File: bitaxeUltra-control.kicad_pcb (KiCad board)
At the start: 4 copper layers, 56.5 x 99.8 mm, 137 parts, among them J1 54-00164, J2 Conn_01x02, J3 Conn_01x05, J4 Conn_01x04, J5 TC2030-IDC, J7 Conn_01x02, J8 USB_C_Receptacle_USB2.0, J9 Conn_01x04, Q1 CSD17311Q5, Q2 CSD17311Q5, Q4 2N7002K, SW1 GT-TC029B-H025-L1N, SW2 GT-TC029B-H025-L1N, U1 25MHz, U10 DS4432U+, U11 RT9080-33GJ5, U12 ESP32-S3-WROOM-1, U14 BM1366_mode1, U2 TXB0104RGYR, U5 MCP1824T-1802E, U6 MCP1824T-0802E, U7 EMC2101, U8 INA260, U9 TPS40305, Y1 32.768kHz

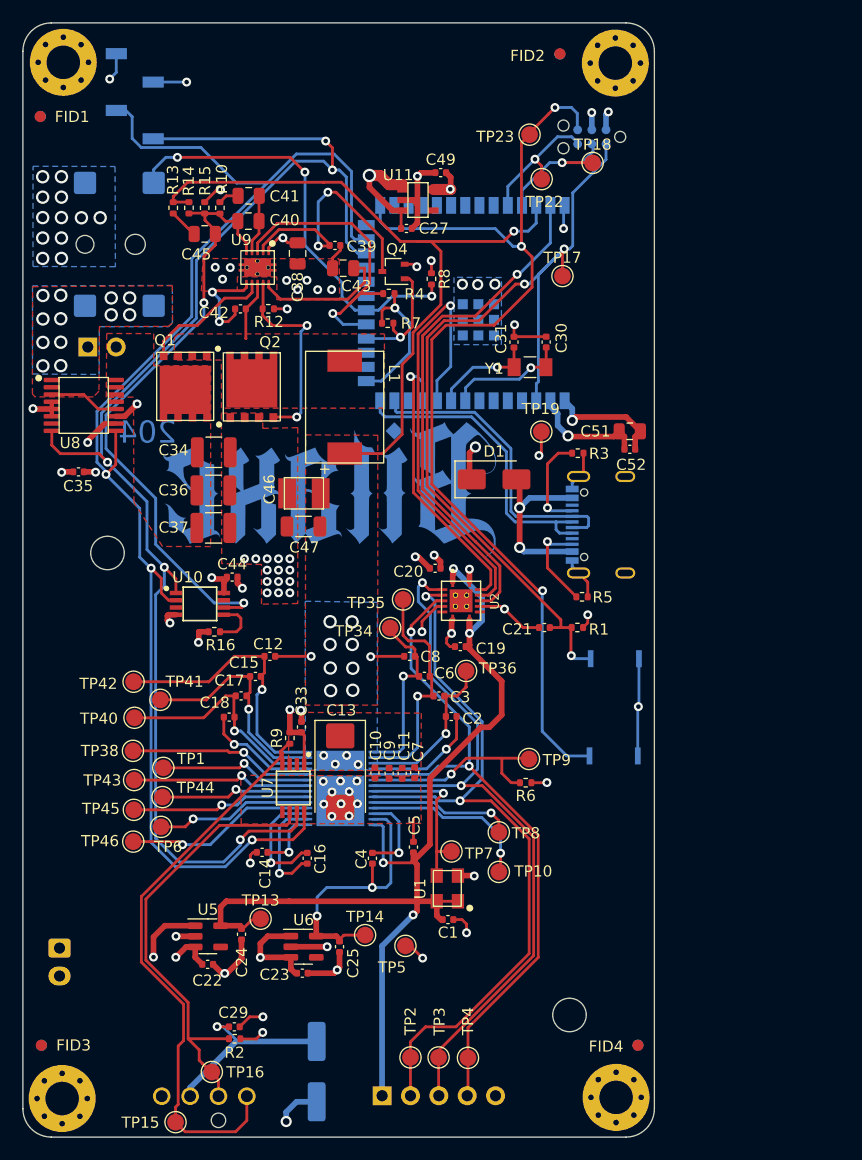
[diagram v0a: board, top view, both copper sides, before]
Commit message: revert  to 4 layer-board routing
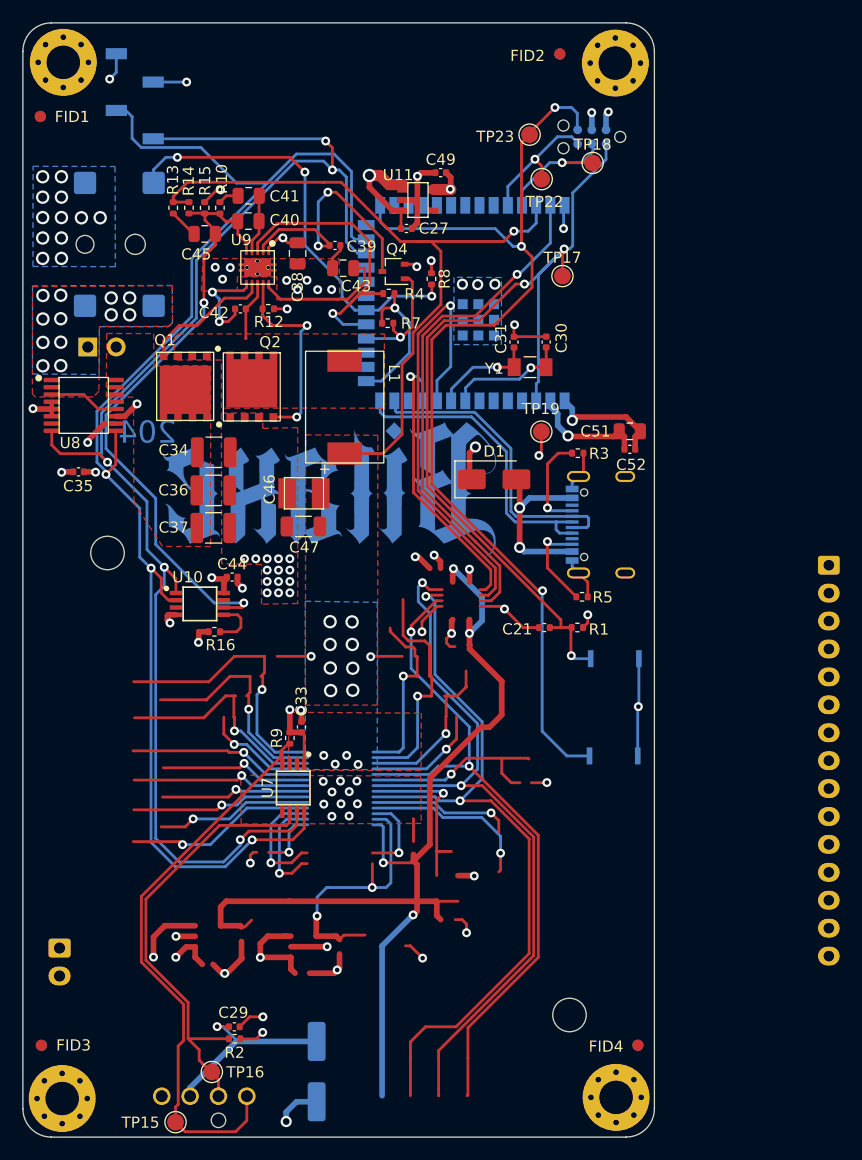
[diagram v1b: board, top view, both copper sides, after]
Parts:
- removed C1, C19, C20, C7, C9: 0.1uF, Capacitor_SMD:C_0402_1005Metric
- removed C10, C11, C12, C14, C15, C16, C17, C18, C2, C22, C23, C24, C25, C3, C4, C5, C6, C8: 1uF, Capacitor_SMD:C_0402_1005Metric
- removed C13: 330uF, Capacitor_Tantalum_SMD:CP_EIA-7343-31_Kemet-D_Pad2.25x2.55mm_HandSolder
- removed R6: 10k, Resistor_SMD:R_0402_1005Metric
- removed TP1, TP10, TP13, TP14, TP2, TP3, TP34, TP35, TP36, TP38, TP4, TP40, TP41, TP42, TP43, TP44, TP45, TP46, TP5, TP6, TP7, TP8, TP9: TestPoint, TestPoint:TestPoint_Pad_D1.5mm
- removed U1: 25MHz, bitaxe:O 25,0-JO32-B-1V3-1-T1-LF
- removed U14: BM1366_mode1, bitaxe:BM1366
- removed U2: TXB0104RGYR, bitaxe:TXB0104
- removed U5: MCP1824T-1802E, Package_TO_SOT_SMD:SOT-23-5
- removed U6: MCP1824T-0802E, Package_TO_SOT_SMD:SOT-23-5
- J3: value Conn_01x05 -> Conn_01x15; footprint Connector_PinHeader_2.54mm:PinHeader_1x05_P2.54mm_Vertical -> Connector_JST:JST_XA_B15B-XASK-1_1x15_P2.50mm_Vertical
- moved J3 62.1 mm to (149.4, 96.1)
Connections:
- J3 pad 1: /BM1366/1V8 -> /RST
- J3 pad 2: /BM1366/CI -> /TX
- J3 pad 3: /BM1366/RO -> /RX
- J3 pad 4: /BM1366/RST_N -> unconnected-(J3-Pin_4-Pad4)
- J3 pad 5: GND -> /5V
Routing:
- net (no net): track 0.00 -> 327.1 mm, vias 0 -> 21
- net /RST: track 46.2 -> 140.3 mm, vias 1 -> 5
- net /BM1366/1V8: track 94.1 -> 0.00 mm, vias 4 -> 0
- net /BM1366/VDD1_1: track 25.2 -> 0.00 mm, vias 1 -> 0
- net /BM1366/0V8: track 24.5 -> 0.00 mm, vias 2 -> 0
- net /BM1366/VDD3_1: track 20.8 -> 0.00 mm, vias 1 -> 0
- net /BM1366/VDD2_0: track 20.7 -> 0.00 mm, vias 1 -> 0
- net /BM1366/VDD2_1: track 20.3 -> 0.00 mm, vias 1 -> 0
- net /BM1366/BI: track 18.2 -> 0.00 mm, vias 1 -> 0
- net /BM1366/PIN_MODE: track 17.1 -> 0.00 mm, vias 1 -> 0
- net /BM1366/NRSTO: track 16.5 -> 0.00 mm, vias 1 -> 0
- net /BM1366/VDD1_0: track 16.2 -> 0.00 mm, vias 1 -> 0
- net /BM1366/RI: track 16.1 -> 0.00 mm, vias 1 -> 0
- net /BM1366/CO: track 16.1 -> 0.00 mm, vias 1 -> 0
- net /BM1366/ADDR1: track 15.7 -> 0.00 mm, vias 1 -> 0
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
